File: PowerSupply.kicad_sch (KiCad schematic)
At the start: 32 parts, among them J901 U.FL-R-SMT(10), J902 U.FL-R-SMT(10), J903 U.FL-R-SMT(10), J904 U.FL-R-SMT(10), J905 U.FL-R-SMT(10), J906 U.FL-R-SMT(10), U901 BAT54W-7-F, U902 ZXCT1009QFTA, U903 LT6233CS6#TRMPBF

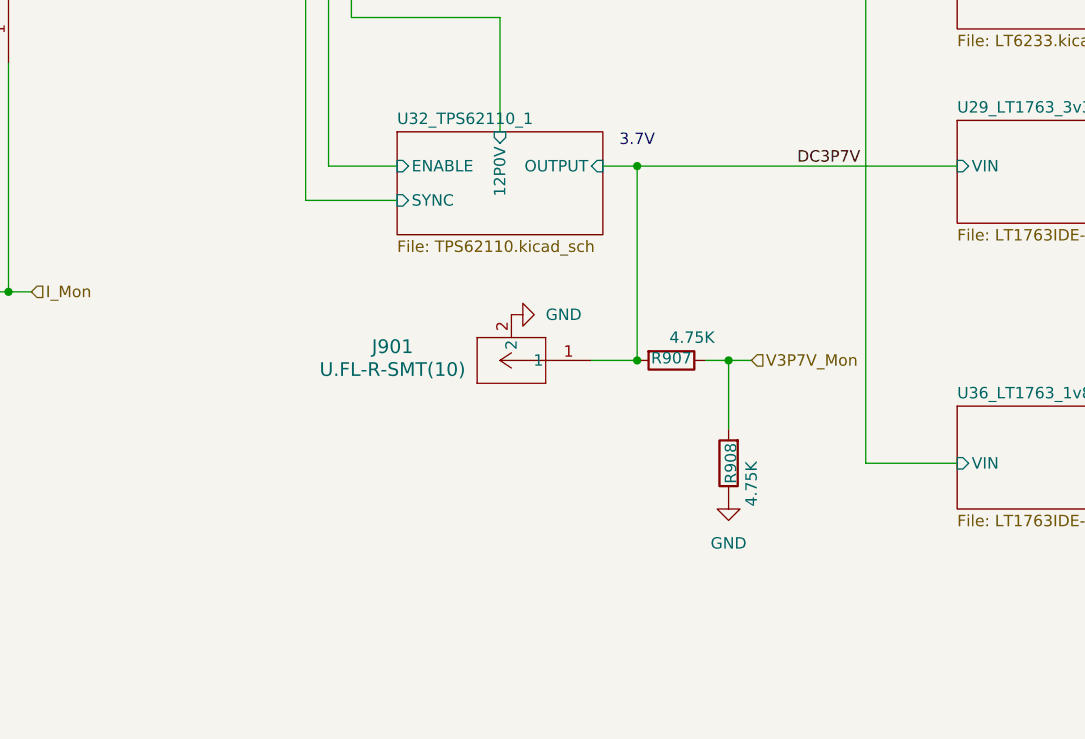
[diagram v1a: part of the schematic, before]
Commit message: Added -3.3V supply, buffer amplifier, and single-to-differential op-amp circuit
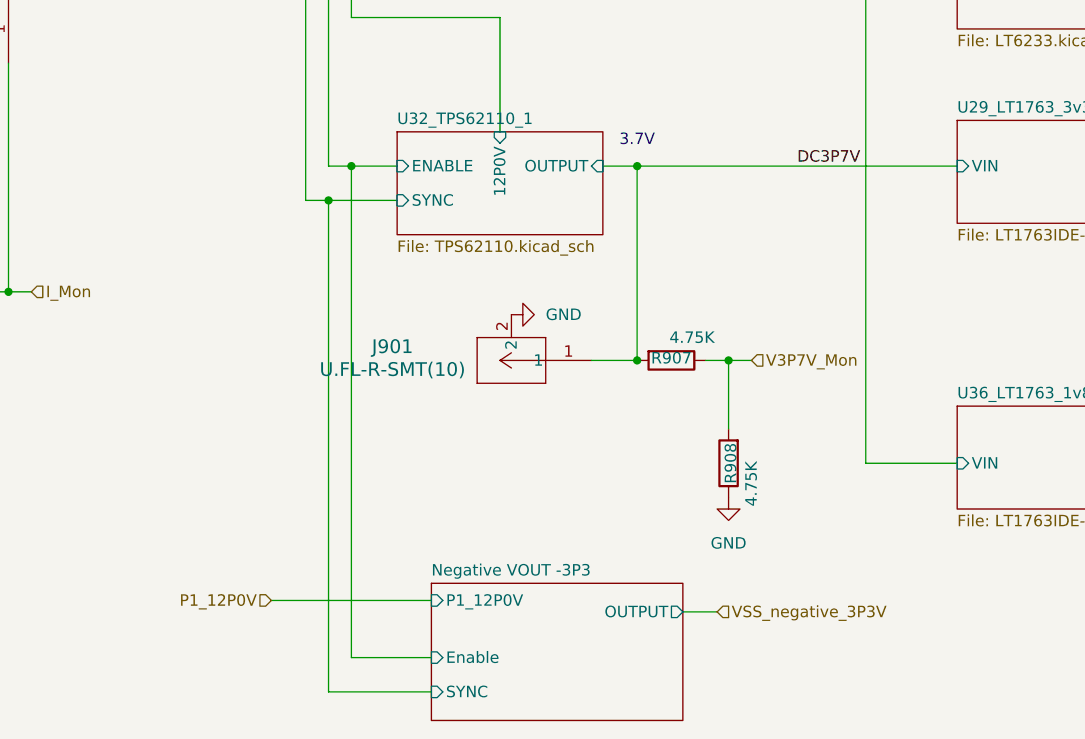
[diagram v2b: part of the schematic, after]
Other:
- added sheet Negative VOUT -3P3 (negativ.kicad_sch)
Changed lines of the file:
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@@
 	)
 	(junction
+		(at 176.53 167.64)
+		(diameter 0)
+		(color 0 0 0 0)
+	)
+	(junction
 		(at 264.16 96.52)
 		(diameter 0)
@@
 	)
 	(junction
+		(at 179.07 163.83)
+		(diameter 0)
+		(color 0 0 0 0)
+	)
+	(junction
 		(at 143.51 101.6)
 		(diameter 0)
@@
 	(wire
 		(pts
+			(xy 176.53 222.25) (xy 187.96 222.25)
+		)
+		(stroke
+			(width 0)
+			(type default)
+		)
+	)
+	(wire
+		(pts
 			(xy 283.21 163.83) (xy 283.21 172.72)
 		)
@@
 	(wire
 		(pts
+			(xy 215.9 213.36) (xy 219.71 213.36)
+		)
+		(stroke
+			(width 0)
+			(type default)
+		)
+	)
+	(wire
+		(pts
 			(xy 279.4 139.7) (xy 322.58 139.7)
 		)
@@
 	(wire
 		(pts
+			(xy 176.53 167.64) (xy 184.15 167.64)
+		)
+		(stroke
+			(width 0)
+			(type default)
+		)
+	)
+	(wire
+		(pts
+			(xy 176.53 167.64) (xy 176.53 222.25)
+		)
+		(stroke
+			(width 0)
+			(type default)
+		)
+	)
+	(wire
+		(pts
 			(xy 270.51 143.51) (xy 279.4 143.51)
 		)
@@
 	(wire
 		(pts
-			(xy 90.17 96.52) (xy 95.25 96.52)
-		)
-		(stroke
-			(width 0)
-			(type default)
-		)
-	)
-	(wire
-		(pts
 			(xy 289.56 91.44) (xy 289.56 83.82)
 		)
@@
 	(wire
 		(pts
-			(xy 176.53 163.83) (xy 184.15 163.83)
+			(xy 176.53 163.83) (xy 179.07 163.83)
 		)
 		(stroke
@@
 	(wire
 		(pts
+			(xy 179.07 163.83) (xy 184.15 163.83)
+		)
+		(stroke
+			(width 0)
+			(type default)
+		)
+	)
+	(wire
+		(pts
 			(xy 180.34 81.28) (xy 180.34 72.39)
 		)
@@
 	(wire
 		(pts
+			(xy 170.18 212.09) (xy 187.96 212.09)
+		)
+		(stroke
+			(width 0)
+			(type default)
+		)
+	)
+	(wire
+		(pts
 			(xy 280.67 196.85) (xy 295.91 196.85)
 		)
@@
 	(wire
 		(pts
-			(xy 173.99 167.64) (xy 184.15 167.64)
+			(xy 173.99 167.64) (xy 176.53 167.64)
 		)
 		(stroke
@@
 	(wire
 		(pts
+			(xy 90.17 96.52) (xy 95.25 96.52)
+		)
+		(stroke
+			(width 0)
+			(type default)
+		)
+	)
+	(wire
+		(pts
 			(xy 283.21 163.83) (xy 298.45 163.83)
 		)
@@
 	(wire
 		(pts
+			(xy 179.07 218.44) (xy 187.96 218.44)
+		)
+		(stroke
+			(width 0)
+			(type default)
+		)
+	)
+	(wire
+		(pts
+			(xy 179.07 163.83) (xy 179.07 218.44)
+		)
+		(stroke
+			(width 0)
+			(type default)
+		)
+	)
+	(wire
+		(pts
 			(xy 102.87 81.28) (xy 180.34 81.28)
 		)
@@
 		)
 	)
+	(hierarchical_label "VSS_negative_3P3V"
+		(shape input)
+		(at 219.71 213.36 0)
+		(fields_autoplaced yes)
+		(effects
+			(font
+				(size 1.27 1.27)
+			)
+			(justify left)
+		)
+	)
 	(hierarchical_label "P2_12P0V"
 		(shape input)
@@
 		)
 	)
+	(hierarchical_label "P1_12P0V"
+		(shape input)
+		(at 170.18 212.09 180)
+		(fields_autoplaced yes)
+		(effects
+			(font
+				(size 1.27 1.27)
+			)
+			(justify right)
+		)
+	)
 	(hierarchical_label "PWR_EN"
 		(shape input)
@@
 			)
 		)
+	)
+	(sheet
+		(at 187.96 210.185)
+		(size 27.94 15.24)
+		(fields_autoplaced yes)
+		(stroke
+			(width 0.1524)
+			(type solid)
+		)
+		(fill
+			(color 0 0 0 0.0000)
+		)
+		(property "Sheetname" "Negative VOUT -3P3"
+			(at 187.96 209.4734 0)
+			(effects
+				(font
+					(size 1.27 1.27)
+				)
+				(justify left bottom)
+			)
+		)
+		(property "Sheetfile" "negativ.kicad_sch"
+			(at 187.96 226.0096 0)
+			(effects
+				(font
+					(size 1.27 1.27)
+				)
+				(justify left top)
+				(hide yes)
+			)
+		)
+		(pin "SYNC" input
+			(at 187.96 222.25 180)
+			(effects
+				(font
+					(size 1.27 1.27)
+				)
+				(justify left)
+			)
+		)
+		(pin "P1_12P0V" input
+			(at 187.96 212.09 180)
+			(effects
+				(font
+					(size 1.27 1.27)
+				)
+				(justify left)
+			)
+		)
+		(pin "OUTPUT" output
+			(at 215.9 213.36 0)
+			(effects
+				(font
+					(size 1.27 1.27)
+				)
+				(justify right)
+			)
+		)
+		(pin "Enable" input
+			(at 187.96 218.44 180)
+			(effects
+				(font
+					(size 1.27 1.27)
+				)
+				(justify left)
+			)
+		)
+		(instances
+			(project "zest"
+				(path "/00000000-0000-0000-0000-000000000003/00000000-0000-0000-0000-000000000002"
+					(page "37")
+				)
+			)
+		)

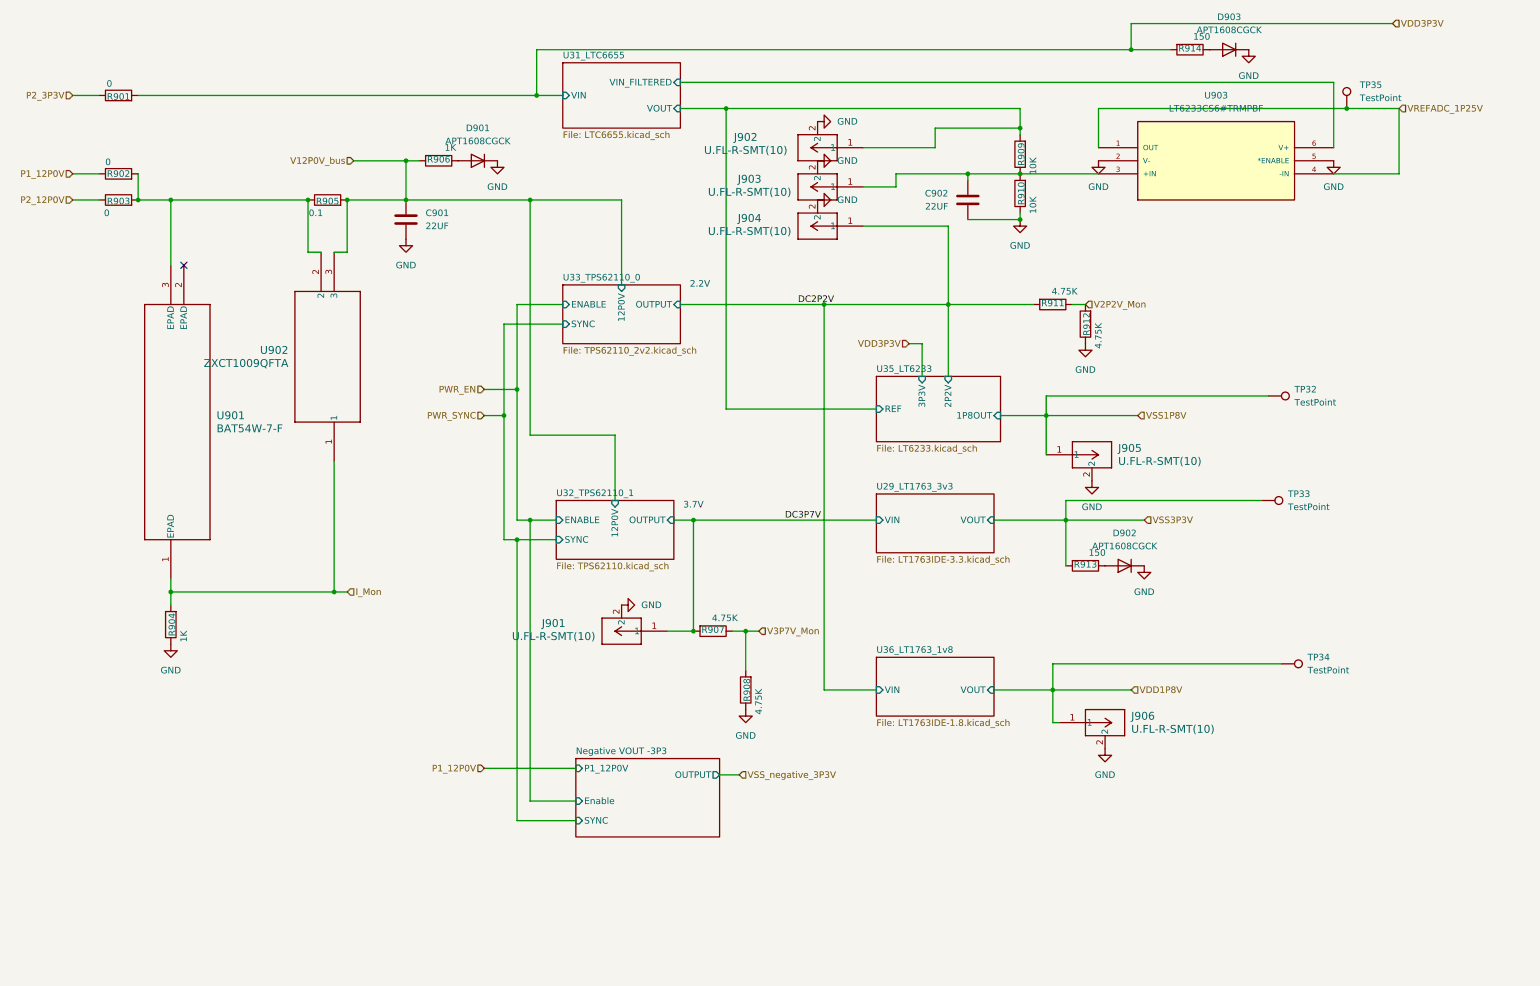
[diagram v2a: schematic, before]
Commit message: Revert FMC connector edge cuts to main version, replace synchronized DC-DC converter with LM2776 (2MHz unsynchronized)
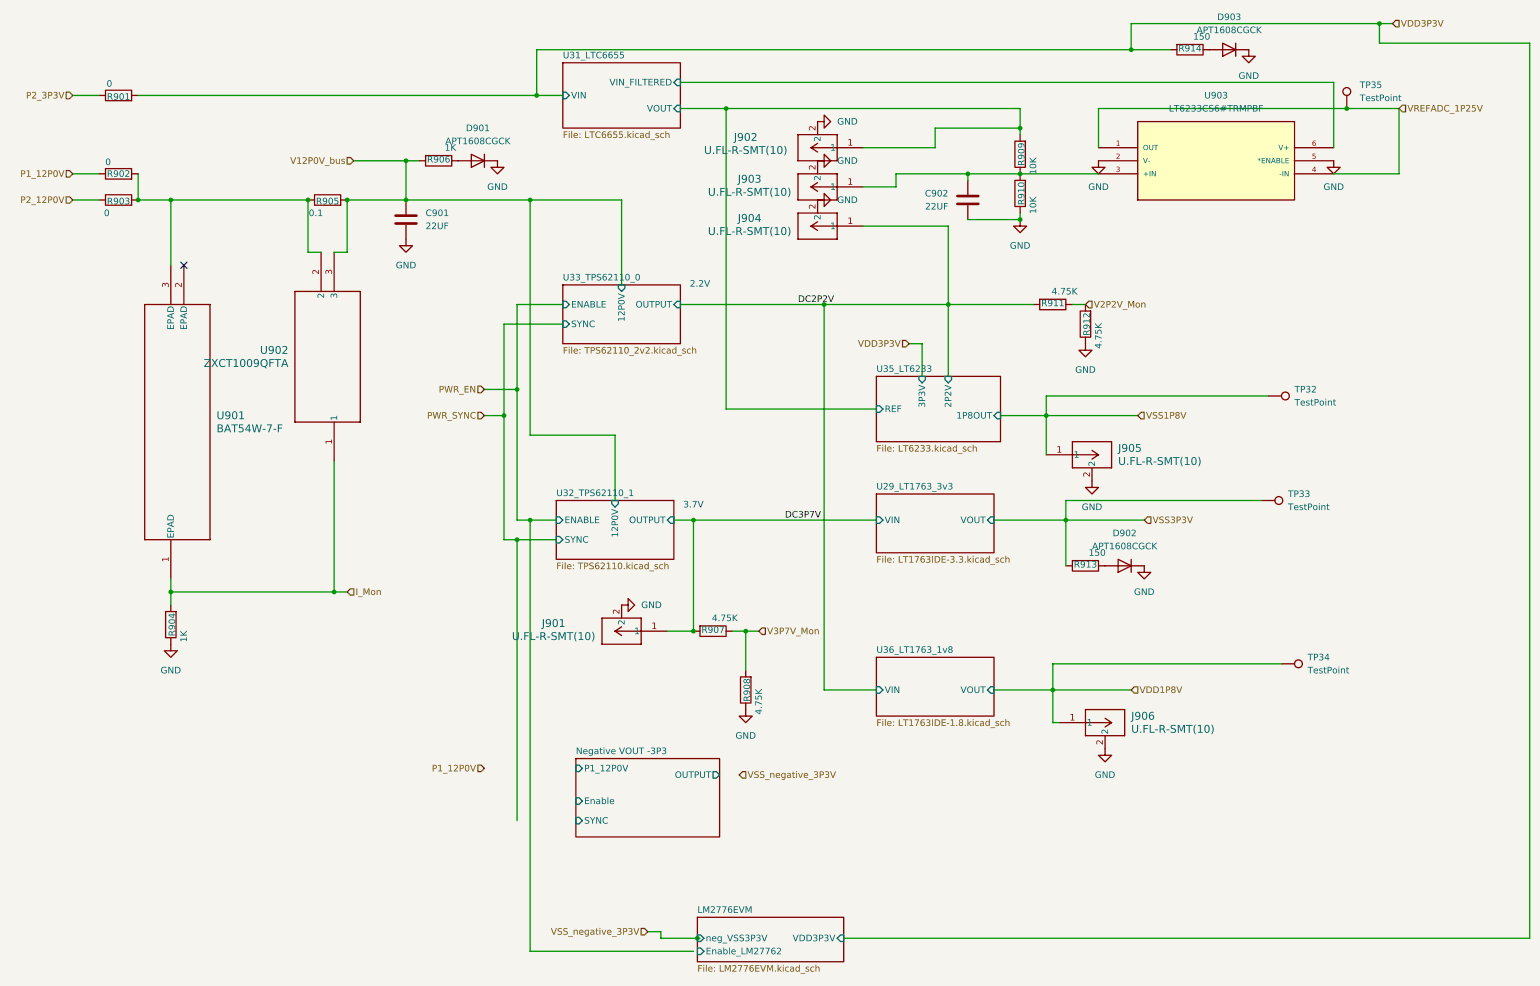
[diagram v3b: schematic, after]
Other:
- added sheet LM2776EVM (LM2776EVM.kicad_sch)
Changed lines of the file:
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@@
 	)
 	(junction
+		(at 344.17 67.31)
+		(diameter 0)
+		(color 0 0 0 0)
+	)
+	(junction
 		(at 102.87 101.6)
 		(diameter 0)
@@
 	)
 	(junction
+		(at 211.582 245.11)
+		(diameter 0)
+		(color 0 0 0 0)
+	)
+	(junction
 		(at 264.16 96.52)
 		(diameter 0)
@@
 	(wire
 		(pts
+			(xy 344.17 71.12) (xy 373.38 71.12)
+		)
+		(stroke
+			(width 0)
+			(type default)
+		)
+	)
+	(wire
+		(pts
 			(xy 109.22 101.6) (xy 109.22 114.3)
 		)
@@
 	(wire
 		(pts
-			(xy 176.53 222.25) (xy 187.96 222.25)
+			(xy 283.21 163.83) (xy 283.21 172.72)
 		)
 		(stroke
@@
 	(wire
 		(pts
-			(xy 283.21 163.83) (xy 283.21 172.72)
+			(xy 373.38 71.12) (xy 373.38 245.11)
 		)
 		(stroke
@@
 	(wire
 		(pts
-			(xy 215.9 213.36) (xy 219.71 213.36)
+			(xy 212.09 245.11) (xy 211.582 245.11)
 		)
 		(stroke
@@
 	(wire
 		(pts
-			(xy 295.91 67.31) (xy 346.71 67.31)
+			(xy 295.91 67.31) (xy 344.17 67.31)
+		)
+		(stroke
+			(width 0)
+			(type default)
+		)
+	)
+	(wire
+		(pts
+			(xy 204.47 243.84) (xy 201.93 243.84)
 		)
 		(stroke
@@
 	(wire
 		(pts
+			(xy 204.47 245.11) (xy 204.47 243.84)
+		)
+		(stroke
+			(width 0)
+			(type default)
+		)
+	)
+	(wire
+		(pts
 			(xy 236.22 196.85) (xy 246.38 196.85)
 		)
@@
 	(wire
 		(pts
+			(xy 240.03 245.11) (xy 373.38 245.11)
+		)
+		(stroke
+			(width 0)
+			(type default)
+		)
+	)
+	(wire
+		(pts
 			(xy 264.16 105.41) (xy 274.32 105.41)
 		)
@@
 	(wire
 		(pts
+			(xy 211.582 245.11) (xy 204.47 245.11)
+		)
+		(stroke
+			(width 0)
+			(type default)
+		)
+	)
+	(wire
+		(pts
 			(xy 217.17 83.82) (xy 217.17 142.24)
 		)
@@
 	(wire
 		(pts
+			(xy 210.82 247.65) (xy 179.07 247.65)
+		)
+		(stroke
+			(width 0)
+			(type default)
+		)
+	)
+	(wire
+		(pts
 			(xy 260.35 121.92) (xy 260.35 135.89)
 		)
@@
 	(wire
 		(pts
-			(xy 170.18 212.09) (xy 187.96 212.09)
+			(xy 280.67 196.85) (xy 295.91 196.85)
 		)
 		(stroke
@@
 	(wire
 		(pts
-			(xy 280.67 196.85) (xy 295.91 196.85)
+			(xy 347.98 83.82) (xy 347.98 96.52)
 		)
 		(stroke
@@
 	(wire
 		(pts
-			(xy 347.98 83.82) (xy 347.98 96.52)
+			(xy 205.74 185.42) (xy 210.82 185.42)
 		)
 		(stroke
@@
 	(wire
 		(pts
-			(xy 205.74 185.42) (xy 210.82 185.42)
+			(xy 176.53 138.43) (xy 176.53 163.83)
 		)
 		(stroke
@@
 	(wire
 		(pts
-			(xy 176.53 138.43) (xy 176.53 163.83)
+			(xy 283.21 160.02) (xy 321.31 160.02)
 		)
 		(stroke
@@
 	(wire
 		(pts
-			(xy 283.21 160.02) (xy 321.31 160.02)
+			(xy 140.97 111.76) (xy 143.51 111.76)
 		)
 		(stroke
@@
 	(wire
 		(pts
-			(xy 140.97 111.76) (xy 143.51 111.76)
+			(xy 173.99 167.64) (xy 176.53 167.64)
 		)
 		(stroke
@@
 	(wire
 		(pts
-			(xy 173.99 167.64) (xy 176.53 167.64)
+			(xy 344.17 67.31) (xy 344.17 71.12)
 		)
 		(stroke
@@
 	(wire
 		(pts
-			(xy 279.4 139.7) (xy 279.4 143.51)
+			(xy 344.17 67.31) (xy 346.71 67.31)
 		)
 		(stroke
@@
 	(wire
 		(pts
-			(xy 143.51 111.76) (xy 143.51 101.6)
+			(xy 279.4 139.7) (xy 279.4 143.51)
 		)
 		(stroke
@@
 	(wire
 		(pts
-			(xy 109.22 180.34) (xy 109.22 177.8)
+			(xy 143.51 111.76) (xy 143.51 101.6)
 		)
 		(stroke
@@
 	(wire
 		(pts
-			(xy 90.17 96.52) (xy 95.25 96.52)
+			(xy 109.22 180.34) (xy 109.22 177.8)
 		)
 		(stroke
@@
 	(wire
 		(pts
-			(xy 283.21 163.83) (xy 298.45 163.83)
+			(xy 90.17 96.52) (xy 95.25 96.52)
 		)
 		(stroke
@@
 	(wire
 		(pts
-			(xy 135.89 101.6) (xy 135.89 111.76)
+			(xy 283.21 163.83) (xy 298.45 163.83)
 		)
 		(stroke
@@
 	(wire
 		(pts
-			(xy 179.07 218.44) (xy 187.96 218.44)
+			(xy 135.89 101.6) (xy 135.89 111.76)
 		)
 		(stroke
@@
 	(wire
 		(pts
-			(xy 179.07 163.83) (xy 179.07 218.44)
+			(xy 179.07 163.83) (xy 179.07 247.65)
 		)
 		(stroke
@@
 		)
 	)
+	(hierarchical_label "VSS_negative_3P3V"
+		(shape input)
+		(at 201.93 243.84 180)
+		(fields_autoplaced yes)
+		(effects
+			(font
+				(size 1.27 1.27)
+			)
+			(justify right)
+		)
+	)
 	(hierarchical_label "V3P7V_Mon"
 		(shape input)
@@
 			)
 		)
+	)
+	(sheet
+		(at 211.582 241.046)
+		(size 28.448 8.636)
+		(fields_autoplaced yes)
+		(stroke
+			(width 0.1524)
+			(type solid)
+		)
+		(fill
+			(color 0 0 0 0.0000)
+		)
+		(property "Sheetname" "LM2776EVM"
+			(at 211.582 240.3344 0)
+			(effects
+				(font
+					(size 1.27 1.27)
+				)
+				(justify left bottom)
+			)
+		)
+		(property "Sheetfile" "LM2776EVM.kicad_sch"
+			(at 211.582 250.2666 0)
+			(effects
+				(font
+					(size 1.27 1.27)
+				)
+				(justify left top)
+			)
+		)
+		(pin "neg_VSS3P3V" input
+			(at 211.582 245.11 180)
+			(effects
+				(font
+					(size 1.27 1.27)
+				)
+				(justify left)
+			)
+		)
+		(pin "Enable_LM27762" input
+			(at 211.582 247.65 180)
+			(effects
+				(font
+					(size 1.27 1.27)
+				)
+				(justify left)
+			)
+		)
+		(pin "VDD3P3V" input
+			(at 240.03 245.11 0)
+			(effects
+				(font
+					(size 1.27 1.27)
+				)
+				(justify right)
+			)
+		)
+		(instances
+			(project "zest"
+				(path "/00000000-0000-0000-0000-000000000003/00000000-0000-0000-0000-000000000002"
+					(page "38")
+				)
+			)
+		)
